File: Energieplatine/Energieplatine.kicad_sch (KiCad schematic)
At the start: 13 parts, among them J1 USB_C_Receptacle_PowerOnly_6P, J2 Conn_01x02_Pin, U1 4027, U2 TL072, U3 LM2576HVT-ADJ

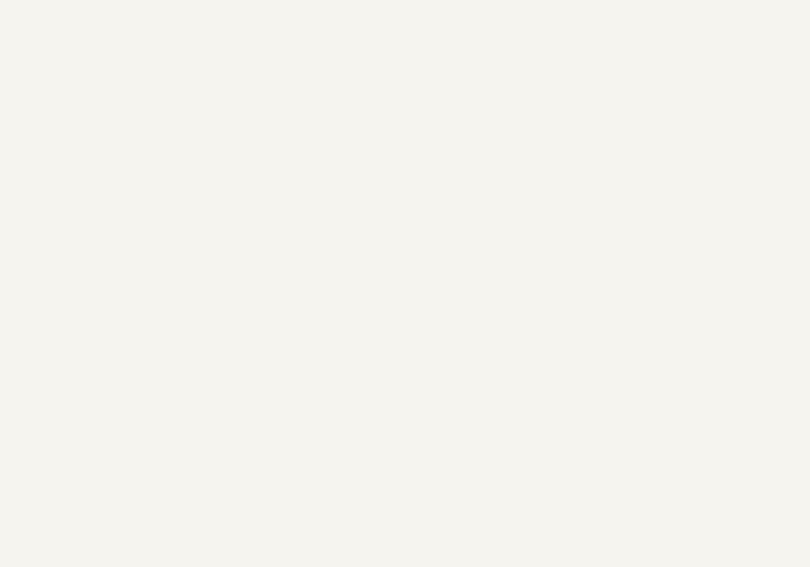
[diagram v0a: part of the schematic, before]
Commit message: Added Resistor
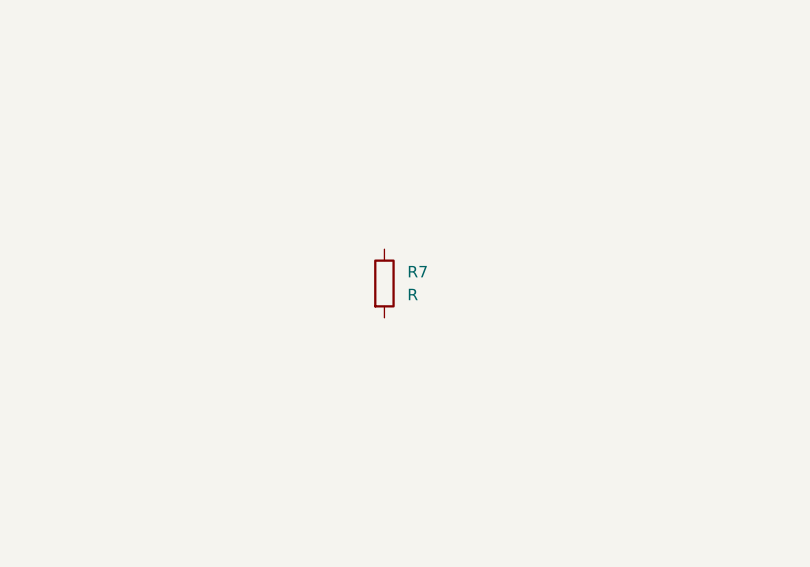
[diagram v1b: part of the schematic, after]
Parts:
- added R7: R, symbol Device:R
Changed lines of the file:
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@@
+	)
+	(symbol
+		(lib_id "Device:R")
+		(at 148.59 92.71 0)
+		(unit 1)
+		(exclude_from_sim no)
+		(in_bom yes)
+		(on_board yes)
+		(dnp no)
+		(fields_autoplaced yes)
+		(property "Reference" "R7"
+			(at 151.13 91.4399 0)
+			(effects
+				(font
+					(size 1.27 1.27)
+				)
+				(justify left)
+			)
+		)
+		(property "Value" "R"
+			(at 151.13 93.9799 0)
+			(effects
+				(font
+					(size 1.27 1.27)
+				)
+				(justify left)
+			)
+		)
+		(property "Footprint" ""
+			(at 146.812 92.71 90)
+			(effects
+				(font
+					(size 1.27 1.27)
+				)
+				(hide yes)
+			)
+		)
+		(property "Datasheet" "~"
+			(at 148.59 92.71 0)
+			(effects
+				(font
+					(size 1.27 1.27)
+				)
+				(hide yes)
+			)
+		)
+		(property "Description" "Resistor"
+			(at 148.59 92.71 0)
+			(effects
+				(font
+					(size 1.27 1.27)
+				)
+				(hide yes)
+			)
+		)
+		(pin "2"
+		)
+		(pin "1"
+		)
+		(instances
+			(project ""
+				(path "/03a54101-e95a-4ac4-b362-52e71af40d1b"
+					(reference "R7")
+					(unit 1)
+				)
+			)
+		)
 	)
 	(symbol

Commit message: widerstand entfernt
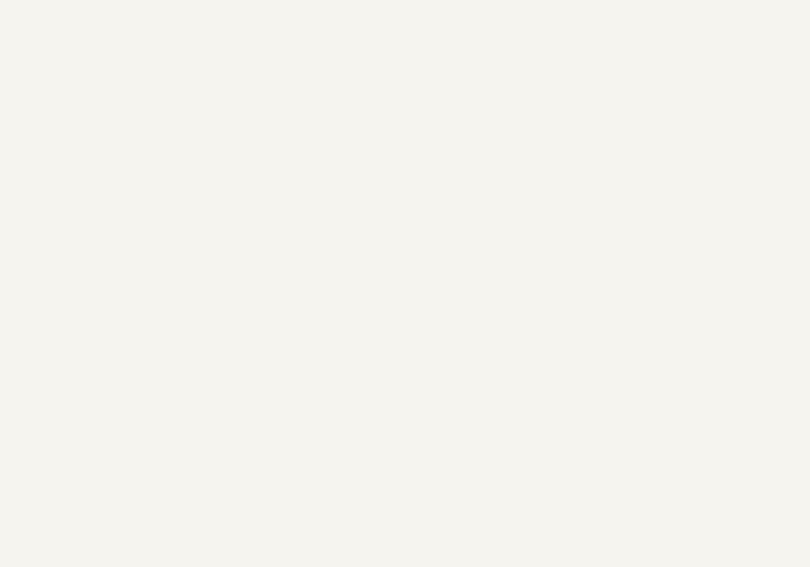
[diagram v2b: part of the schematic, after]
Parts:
- removed R7: R, symbol Device:R
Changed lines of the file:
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@@
-	)
-	(symbol
-		(lib_id "Device:R")
-		(at 148.59 92.71 0)
-		(unit 1)
-		(exclude_from_sim no)
-		(in_bom yes)
-		(on_board yes)
-		(dnp no)
-		(fields_autoplaced yes)
-		(property "Reference" "R7"
-			(at 151.13 91.4399 0)
-			(effects
-				(font
-					(size 1.27 1.27)
-				)
-				(justify left)
-			)
-		)
-		(property "Value" "R"
-			(at 151.13 93.9799 0)
-			(effects
-				(font
-					(size 1.27 1.27)
-				)
-				(justify left)
-			)
-		)
-		(property "Footprint" ""
-			(at 146.812 92.71 90)
-			(effects
-				(font
-					(size 1.27 1.27)
-				)
-				(hide yes)
-			)
-		)
-		(property "Datasheet" "~"
-			(at 148.59 92.71 0)
-			(effects
-				(font
-					(size 1.27 1.27)
-				)
-				(hide yes)
-			)
-		)
-		(property "Description" "Resistor"
-			(at 148.59 92.71 0)
-			(effects
-				(font
-					(size 1.27 1.27)
-				)
-				(hide yes)
-			)
-		)
-		(pin "2"
-		)
-		(pin "1"
-		)
-		(instances
-			(project ""
-				(path "/03a54101-e95a-4ac4-b362-52e71af40d1b"
-					(reference "R7")
-					(unit 1)
-				)
-			)
-		)
 	)
 	(symbol

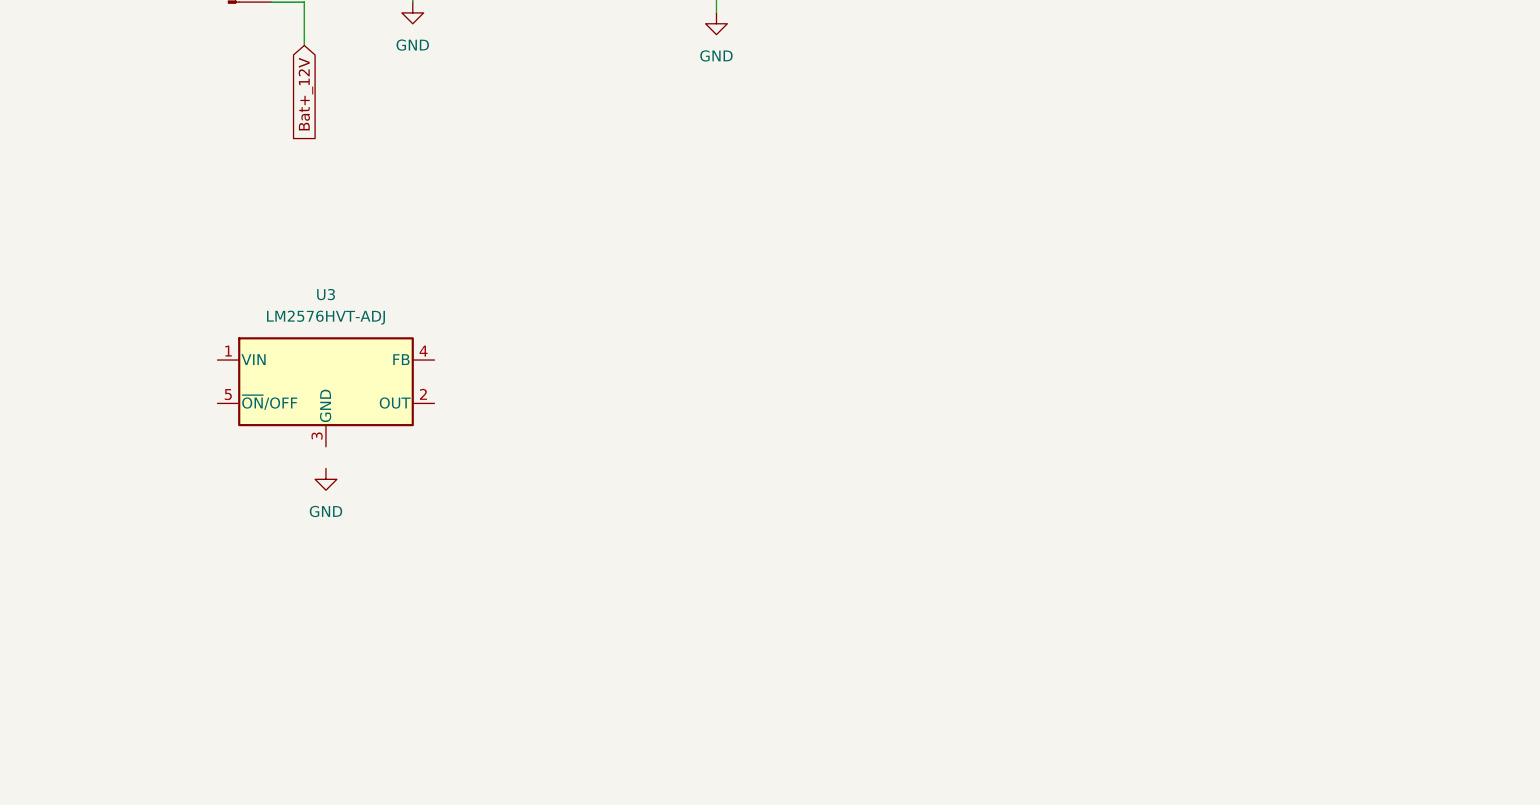
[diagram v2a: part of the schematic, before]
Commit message: Added Boost-Converter
Boost Converter to charge the battery. 5V to 13.8V
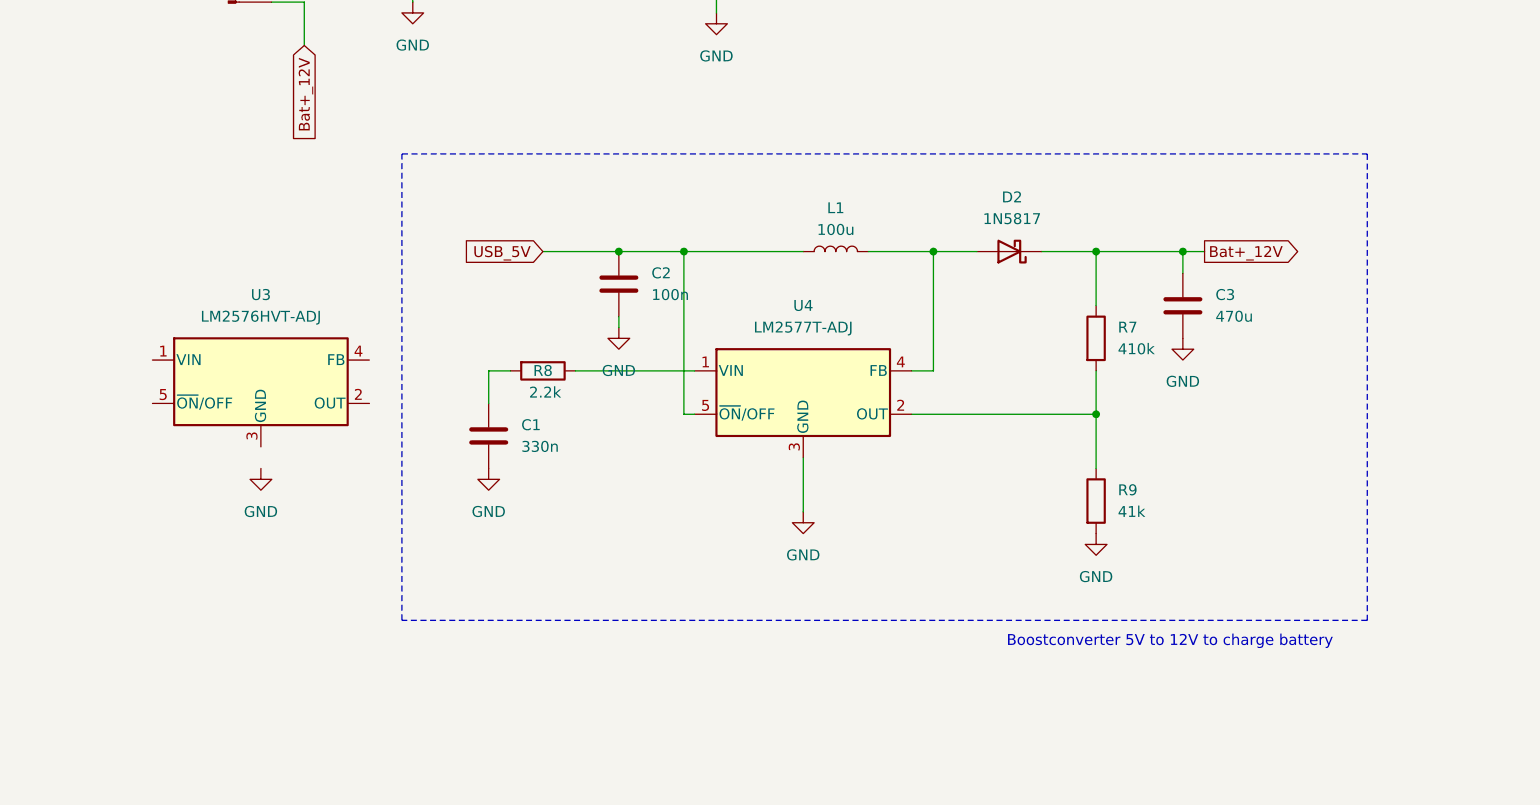
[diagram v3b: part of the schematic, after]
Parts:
- added C1: 330n, symbol Device:C
- added C2: 100n, symbol Device:C
- added C3: 470u, symbol Device:C
- added D2: 1N5817, Diode_THT:D_DO-41_SOD81_P10.16mm_Horizontal, symbol Diode:1N5817
- added L1: 100u, symbol Device:L
- added R7: 410k, symbol Device:R
- added R8: 2.2k, symbol Device:R
- added R9: 41k, symbol Device:R
- added U4: LM2577T-ADJ, Package_TO_SOT_THT:TO-220-5_Vertical, symbol Regulator_Switching:LM2576HVT-ADJ
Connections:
- net Bat+_12V: now also C3.1, D2.1 (K), R7.1
- net GND: now also C1.2, C2.2, C3.2, R9.2, U4.3 (GND)
- net USB_5V: now also C2.1, L1.1, U4.5 (~{ON}/OFF)
- new net: R8.1, U4.1 (VIN)
- new net: C1.1, R8.2
- new net: D2.2 (A), L1.2, U4.4 (FB)
- new net: R7.2, R9.1, U4.2 (OUT)
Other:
- note added: "Boostconverter 5V to 12V to charge battery"
- moved on the sheet: U3

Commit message: Update Energieplatine.kicad_sch
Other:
- note added: "Boost-Converter to charge the battery"
- note removed: "Boostconverter 5V to 12V to charge battery"
- moved on the sheet: C1, C2, C3, D2, L1, R7, R8, R9, U3, U4
